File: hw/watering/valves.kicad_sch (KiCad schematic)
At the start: 8 parts, among them J4 Conn_01x02_Pin, U6 STI3508

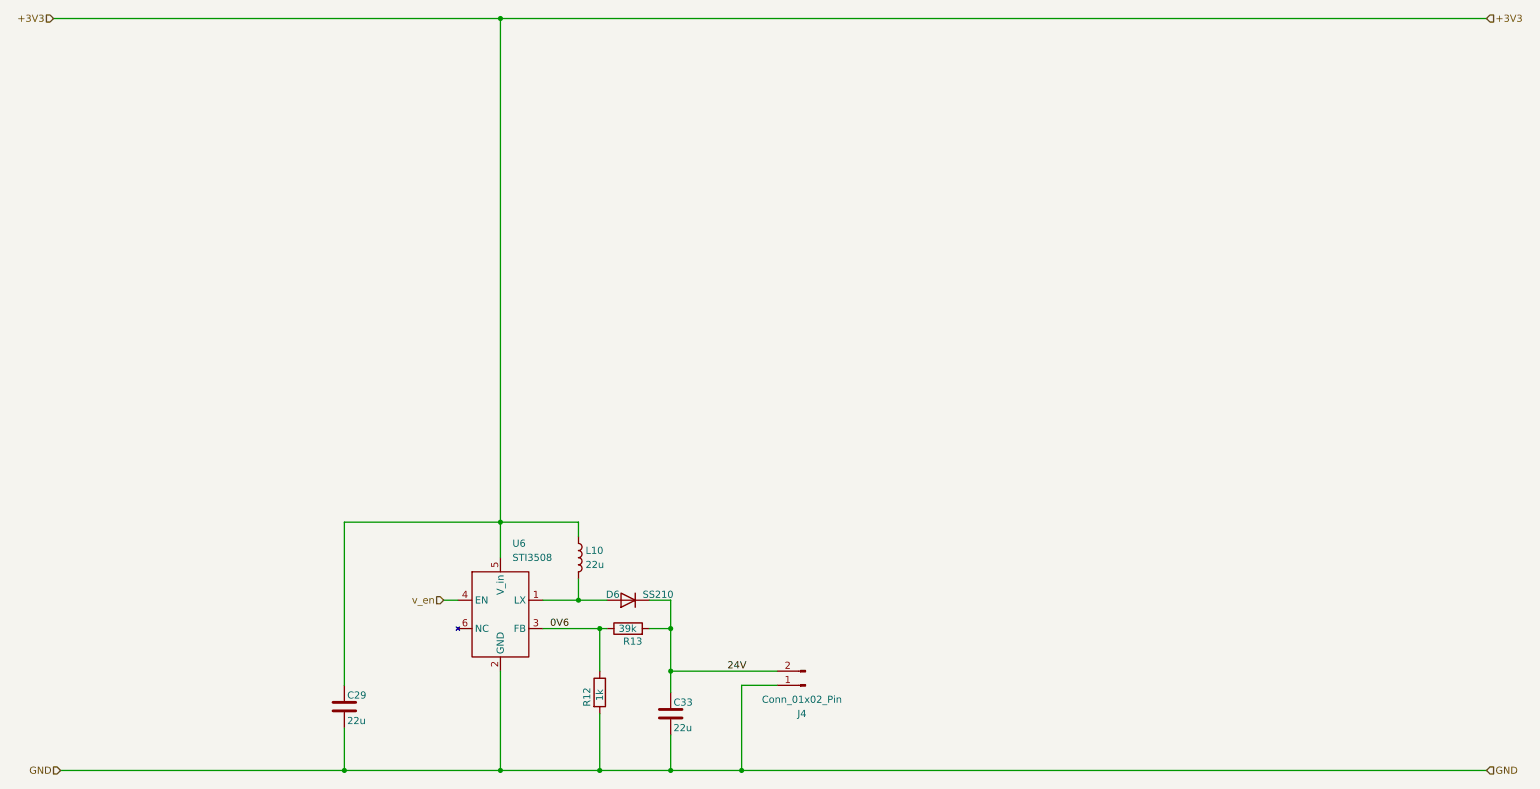
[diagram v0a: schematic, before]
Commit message: - hw   - rewired power input for battery   - some first placing of parts on pcb but no routing - sw   - added example http server from examples to server.cpp, not compilable yet
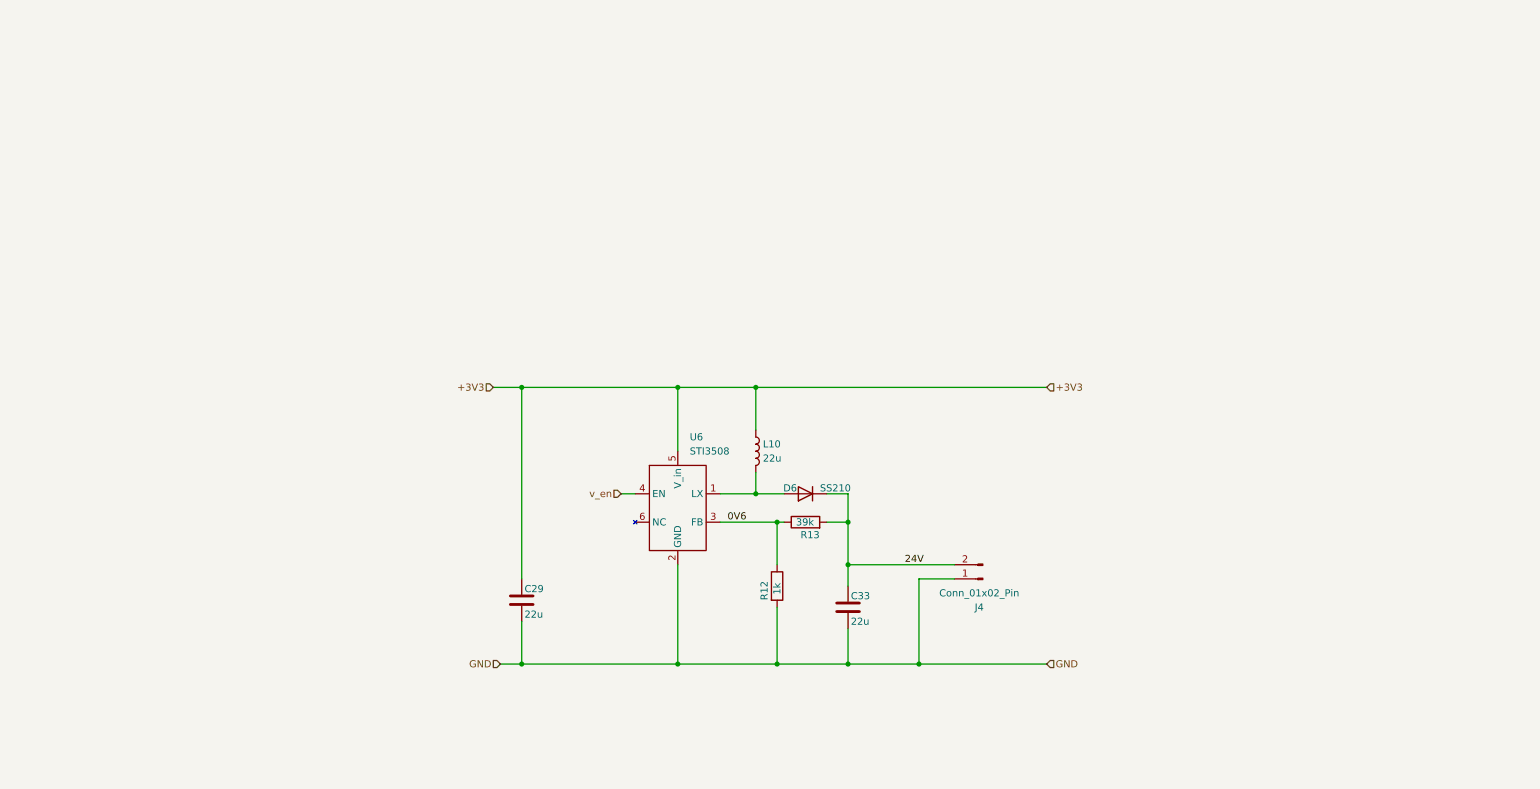
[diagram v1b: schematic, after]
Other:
- moved on the sheet: C29, C33, D6, J4, L10, R12, R13, U6
